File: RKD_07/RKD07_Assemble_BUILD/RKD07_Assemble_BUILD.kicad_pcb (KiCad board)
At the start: 2 copper layers, 233.4 x 200 mm, 174 parts, among them J1 Conn_01x02_Socket, J10 Conn_01x04, J11 TRRS, J12 Conn_01x06, J13 Conn_01x06, J14 Conn_01x04, J15 Conn_01x04, J2 Conn_01x24, J3 Conn_01x24, J4 Conn_01x24, J5 Qwiic_RA, J6 Qwiic_RA, J7 Conn_01x06, J8 Conn_01x06, J9 Conn_01x04, M3 Mark, M4 Mark, M5 Mark, M6 Mark, M8 Mark, SW1 SW_Push, SW10 SW_Push, SW11 SW_Push, SW12 SW_Push, SW13 SW_Push, SW14 SW_Push, SW15 SW_Push, SW16 SW_Push, SW17 SW_Push, SW18 SW_Push, SW19 SW_Push, SW2 SW_Push, SW20 SW_Push, SW21 SW_Push, SW22 SW_Push, SW23 SW_Push, SW24 SW_Push, SW25 SW_Push, SW26 SW_Push, SW27 SW_Push, SW28 SW_Push, SW29 SW_Push, SW3 SW_Push, SW30 RotaryEncoder_Switch, SW31 SW_Push, SW4 SW_Push, SW5 SW_Push, SW51 SW_Push, SW52 SW_Push, SW53 SW_Push, SW54 SW_Push, SW55 SW_Push, SW56 SW_Push, SW57 SW_Push, SW58 SW_Push, SW59 SW_Push, SW6 SW_Push, SW60 SW_Push, SW61 SW_Push, SW62 SW_Push, SW63 SW_Push, SW64 SW_Push, SW65 SW_Push, SW66 SW_Push, SW67 SW_Push, SW68 SW_Push, SW69 SW_Push, SW7 SW_Push, SW70 SW_Push, SW71 SW_Push, SW72 SW_Push, SW73 SW_Push, SW74 SW_Push, SW75 SW_Push, SW76 SW_Push, SW77 SW_Push, SW78 SW_Push, SW79 SW_Push, SW8 SW_Push, SW80 SW_Push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

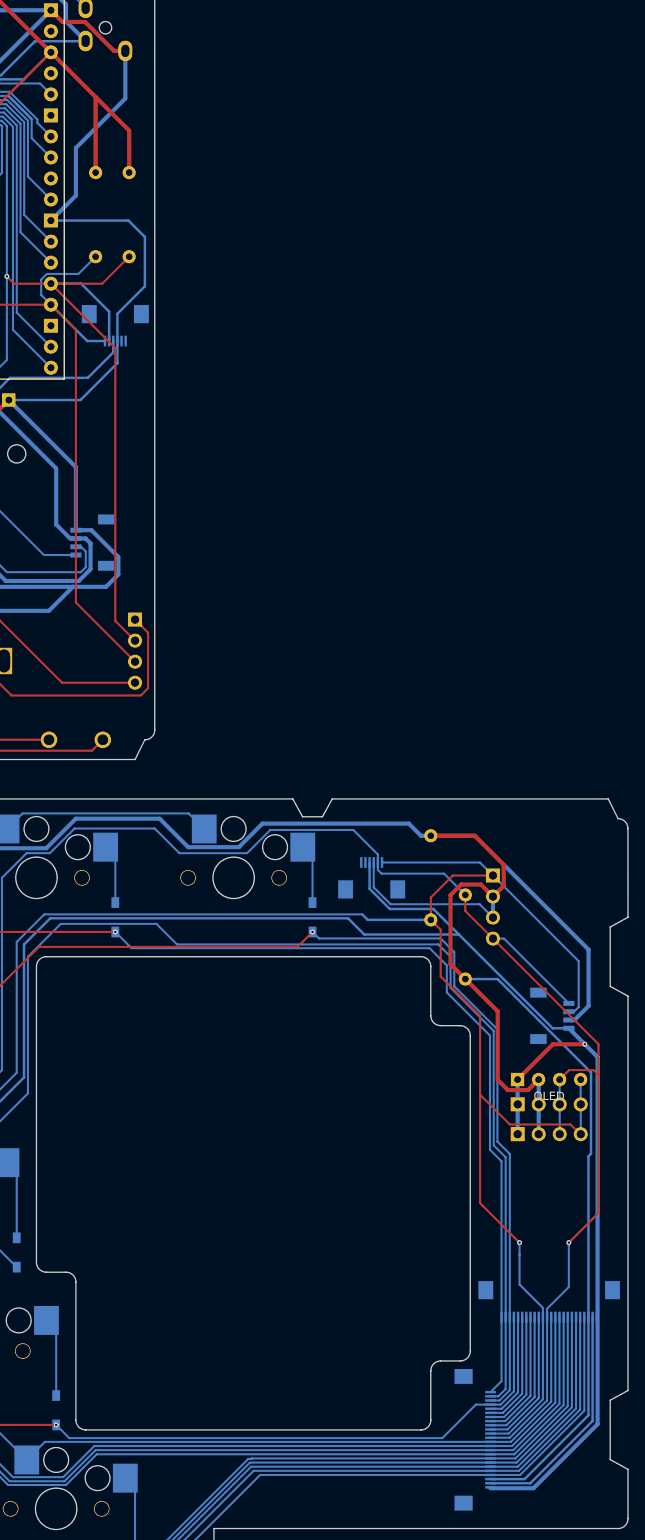
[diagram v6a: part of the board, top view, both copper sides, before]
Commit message: 07 I2Cを整理
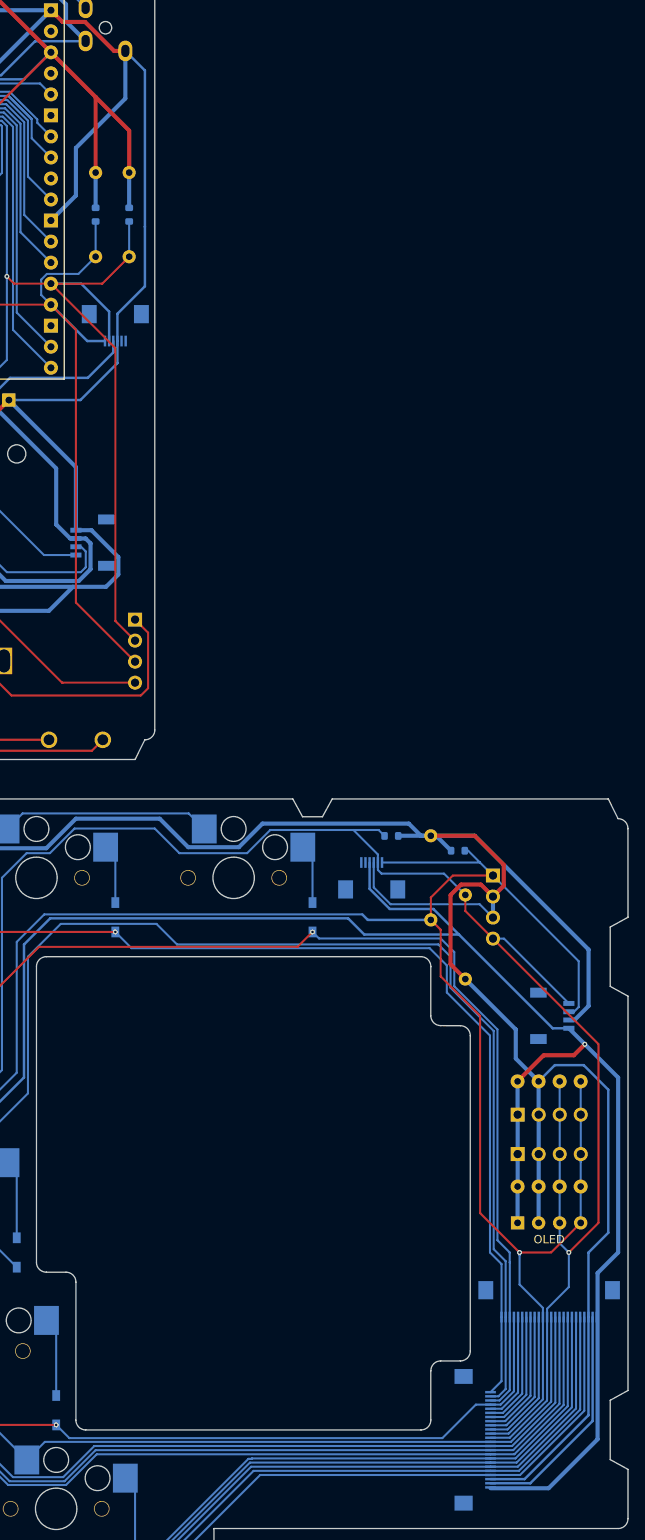
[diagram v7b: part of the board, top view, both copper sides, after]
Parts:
- added OL4: OLED, kicad:AZ1UBALL, B.Cu at (242.9, 164.3)
- added R5: 1kΩ, Resistor_SMD:R_0603_1608Metric, B.Cu at (223.8, 128.3)
- added R6: 1kΩ, Resistor_SMD:R_0603_1608Metric, B.Cu at (231.9, 130.1)
- added R7: 1kΩ, Resistor_SMD:R_0603_1608Metric, B.Cu at (192.2, 53.3)
- added R8: 1kΩ, Resistor_SMD:R_0603_1608Metric, B.Cu at (188.1, 53.3)
- moved OL3 17.3 mm to (242.9, 193.5)
- moved J14 2.41 mm to (239.1, 166.7)
- moved J15 1.24 mm to (239.1, 161.9)
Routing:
- net GND_R: track 207.7 -> 221.4 mm
- net SCL/TX_R: track 203.9 -> 217.1 mm
- net GND_L: track 247.9 -> 259.2 mm
- net 3v3_L: track 217.9 -> 226.4 mm
- net SDA/SCK_R: track 220.6 -> 228.4 mm
- net SCL/TX_L: track 175.9 -> 180.1 mm
- net SDA/SCK_L: track 192.6 -> 196.9 mm
- net 3v3_R: track 288.6 -> 291.9 mm
